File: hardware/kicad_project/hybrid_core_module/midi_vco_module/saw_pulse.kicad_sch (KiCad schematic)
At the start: 8 parts, among them U24 TL074

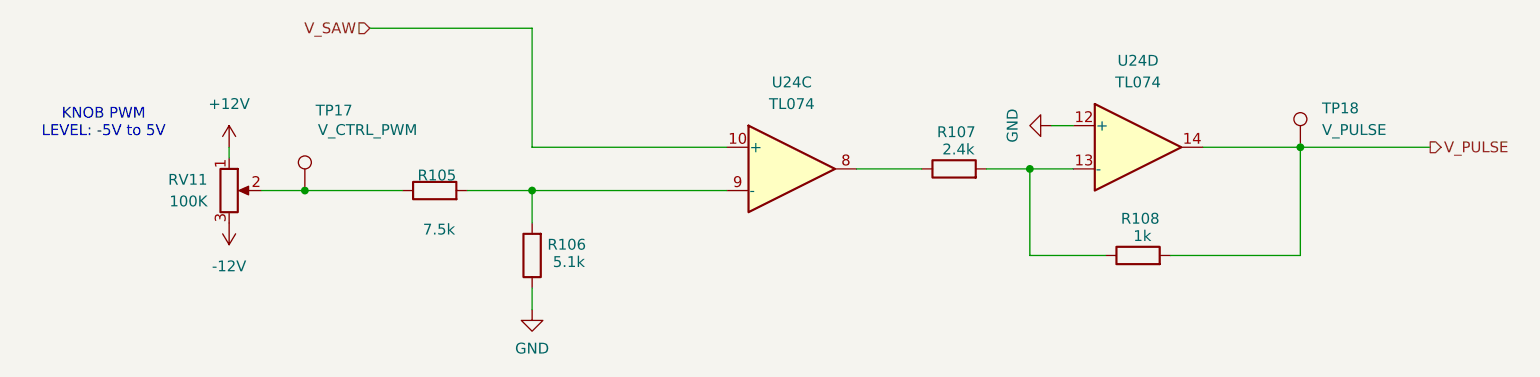
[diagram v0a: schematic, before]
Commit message: Schematic updated. Components Footprint assignment started. Waiting for components mechanical validation before starting layout.
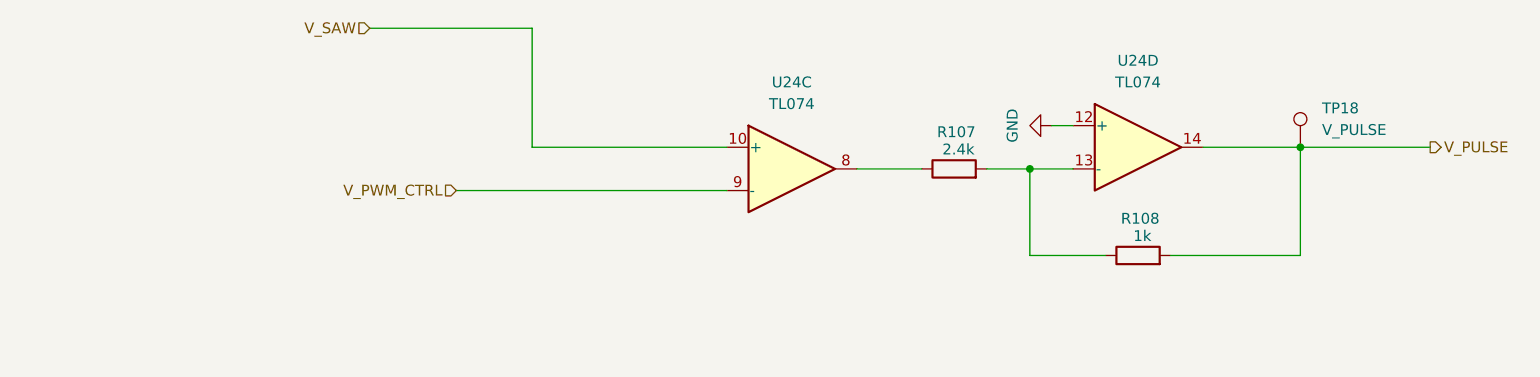
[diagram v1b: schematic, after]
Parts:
- removed R105: 7.5k, symbol Device:R
- removed R106: 5.1k, symbol Device:R
- removed RV11: 100K, symbol Device:R_Potentiometer
- removed TP17: V_CTRL_PWM, symbol Connector:TestPoint
- R107: footprint (none) -> Resistor_SMD:R_0402_1005Metric; Manufacturer (none) -> YAGEO; Manufacturer PartNumer (none) -> RT0402BRD072K4L
- R108: footprint (none) -> Resistor_SMD:R_0402_1005Metric; Manufacturer (none) -> YAGEO; Manufacturer PartNumer (none) -> RT0402FRE071KL
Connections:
- net V_PWM_CTRL: now reaches U24.9 (-)
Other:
- note removed: "KNOB PWM LEVEL: -5V to 5V"

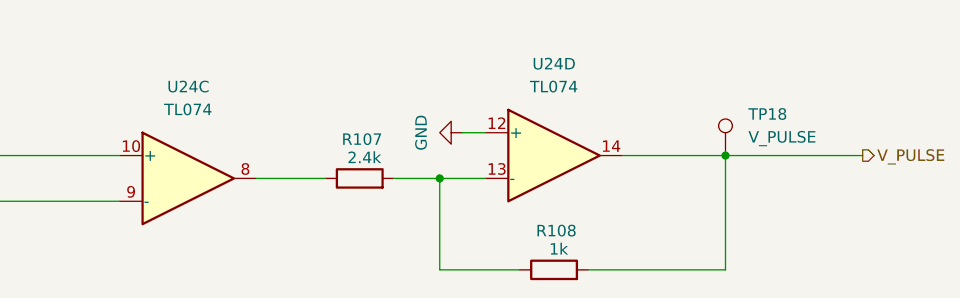
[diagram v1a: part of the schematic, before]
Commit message: - schematic updated  - PN and footprints added
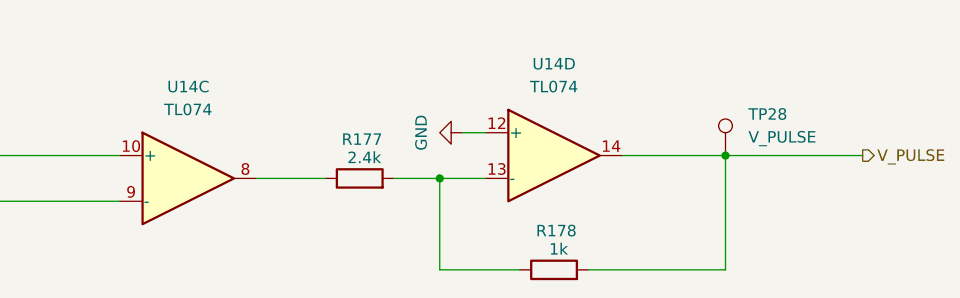
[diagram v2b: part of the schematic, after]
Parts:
- U14: renamed from U24; footprint (none) -> Package_SO:SOIC-14_3.9x8.7mm_P1.27mm; Manufacturer (none) -> Texas Instruments
- renumbered R107 to R177, R108 to R178, TP18 to TP28
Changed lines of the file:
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@@
 		(on_board yes)
 		(dnp no)
-		(property "Reference" "#PWR0246"
+		(property "Reference" "#PWR0313"
 			(at 171.45 71.12 0)
 			(effects
@@
 		(dnp no)
 		(fields_autoplaced yes)
-		(property "Reference" "U24"
+		(property "Reference" "U14"
 			(at 147.32 66.04 0)
 			(effects
@@
 			)
 		)
-		(property "Footprint" ""
+		(property "Footprint" "Package_SO:SOIC-14_3.9x8.7mm_P1.27mm"
 			(at 146.05 73.66 0)
 			(effects
@@
 		)
 		(property "Manufacturer PartNumer" "TL074HIDR"
+			(at 147.32 76.2 0)
+			(effects
+				(font
+					(size 1.27 1.27)
+				)
+				(hide yes)
+			)
+		)
+		(property "MN" ""
+			(at 147.32 76.2 0)
+			(effects
+				(font
+					(size 1.27 1.27)
+				)
+				(hide yes)
+			)
+		)
+		(property "MPN" ""
+			(at 147.32 76.2 0)
+			(effects
+				(font
+					(size 1.27 1.27)
+				)
+				(hide yes)
+			)
+		)
+		(property "Manufacturer" "Texas Instruments"
 			(at 147.32 76.2 0)
 			(effects
@@
 		(on_board yes)
 		(dnp no)
-		(property "Reference" "R107"
+		(property "Reference" "R177"
 			(at 166.624 71.882 90)
 			(effects
@@
 		)
 		(property "Manufacturer PartNumer" "RT0402BRD072K4L"
+			(at 166.37 76.2 90)
+			(effects
+				(font
+					(size 1.27 1.27)
+				)
+				(hide yes)
+			)
+		)
+		(property "MN" ""
+			(at 166.37 76.2 90)
+			(effects
+				(font
+					(size 1.27 1.27)
+				)
+				(hide yes)
+			)
+		)
+		(property "MPN" ""
 			(at 166.37 76.2 90)
 			(effects
@@
 		(dnp no)
 		(fields_autoplaced yes)
-		(property "Reference" "U24"
+		(property "Reference" "U14"
 			(at 187.96 63.5 0)
 			(effects
@@
 			)
 		)
-		(property "Footprint" ""
+		(property "Footprint" "Package_SO:SOIC-14_3.9x8.7mm_P1.27mm"
 			(at 186.69 71.12 0)
 			(effects
@@
 		)
 		(property "Manufacturer PartNumer" "TL074HIDR"
+			(at 187.96 73.66 0)
+			(effects
+				(font
+					(size 1.27 1.27)
+				)
+				(hide yes)
+			)
+		)
+		(property "MN" ""
+			(at 187.96 73.66 0)
+			(effects
+				(font
+					(size 1.27 1.27)
+				)
+				(hide yes)
+			)
+		)
+		(property "MPN" ""
+			(at 187.96 73.66 0)
+			(effects
+				(font
+					(size 1.27 1.27)
+				)
+				(hide yes)
+			)
+		)
+		(property "Manufacturer" "Texas Instruments"
 			(at 187.96 73.66 0)
 			(effects
@@
 		(dnp no)
 		(fields_autoplaced yes)
-		(property "Reference" "TP18"
+		(property "Reference" "TP28"
 			(at 209.55 69.0879 0)
 			(effects
@@
 		)
 		(property "Description" "test point"
+			(at 207.01 73.66 0)
+			(effects
+				(font
+					(size 1.27 1.27)
+				)
+				(hide yes)
+			)
+		)
+		(property "MN" ""
+			(at 207.01 73.66 0)
+			(effects
+				(font
+					(size 1.27 1.27)
+				)
+				(hide yes)
+			)
+		)
+		(property "MPN" ""
 			(at 207.01 73.66 0)
 			(effects
@@
 		(on_board yes)
 		(dnp no)
-		(property "Reference" "R108"
+		(property "Reference" "R178"
 			(at 188.214 82.042 90)
 			(effects
@@
 			(at 187.96 86.36 90)
 			(effects
+				(font
+					(size 1.27 1.27)
+				)
+				(hide yes)
+			)
+		)
+		(property "MN" ""
+			(at 187.96 86.36 90)
+			(effects
+				(font
+					(size 1.27 1.27)
+				)
+				(hide yes)
+			)
+		)
+		(property "MPN" ""
+			(at 187.96 86.36 90)
+			(effects

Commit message: components placement (interface) components placement per section
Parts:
- TP28: footprint (none) -> TestPoint:TestPoint_Pad_1.0x1.0mm
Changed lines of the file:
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@@
 			)
 		)
-		(property "Footprint" ""
+		(property "Footprint" "TestPoint:TestPoint_Pad_1.0x1.0mm"
 			(at 212.09 73.66 0)
 			(effects
